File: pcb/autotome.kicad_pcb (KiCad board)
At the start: 2 copper layers, 61 parts, among them SW1 SW_PUSH, SW10 SW_PUSH, SW11 SW_PUSH, SW12 SW_PUSH, SW13 SW_PUSH, SW14 SW_PUSH, SW15 SW_PUSH, SW16 SW_PUSH, SW17 SW_PUSH, SW18 SW_PUSH, SW19 SW_PUSH, SW2 SW_PUSH, SW20 SW_PUSH, SW21 SW_PUSH, SW22 SW_PUSH, SW23 SW_PUSH, SW24 SW_PUSH, SW25 RotaryEncoder_Switch, SW27 SW_PUSH, SW28 SW_PUSH, SW29 SW_PUSH, SW3 SW_PUSH, SW30 SW_PUSH, SW31 SW_SPDT, SW4 SW_PUSH, SW5 SW_PUSH, SW6 SW_PUSH, SW7 SW_PUSH, SW8 SW_PUSH, SW9 SW_PUSH, U1 ProMicro

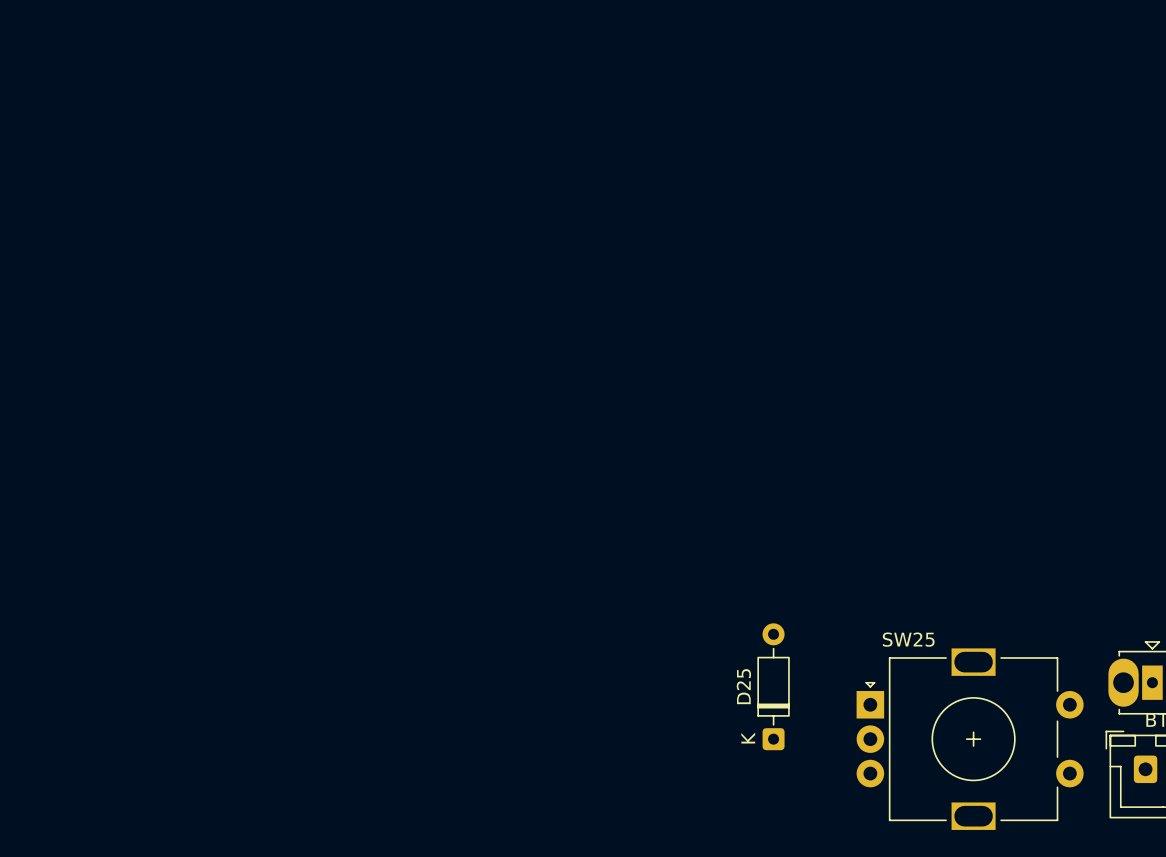
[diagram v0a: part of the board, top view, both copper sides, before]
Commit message: add rotary encoder 3d model and custom library
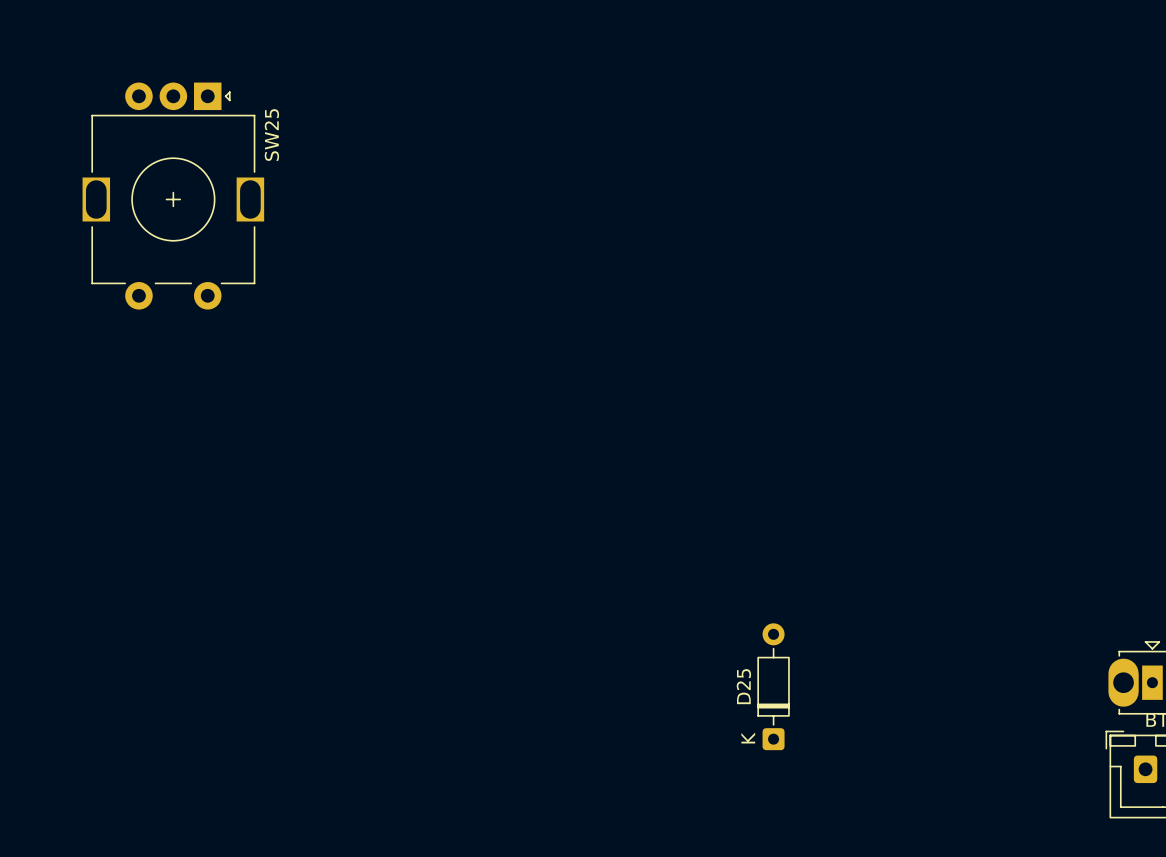
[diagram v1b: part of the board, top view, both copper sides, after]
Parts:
- SW25: footprint Rotary_Encoder:RotaryEncoder_Alps_EC11E-Switch_Vertical_H20mm -> my_library:RotaryEncoder_Alps_EC11E-Switch_Vertical_H20mm
- moved SW25 65.4 mm to (197.0, 115.2), turned to -90 degrees
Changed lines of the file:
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@@
 		(capping no)
 		(filling no)
+		(aux_axis_origin 123.14608 139.584744)
 		(pcbplotparams
 			(layerselection 0x00000000_00000000_55555555_5755f5ff)
@@
 		)
 	)
-	(footprint "Rotary_Encoder:RotaryEncoder_Alps_EC11E-Switch_Vertical_H20mm"
+	(footprint "my_library:RotaryEncoder_Alps_EC11E-Switch_Vertical_H20mm"
 		(layer "F.Cu")
-		(at 245.1625 159.425)
+		(at 197 115.2 -90)
 		(descr "Alps rotary encoder, EC11E... with switch, vertical shaft, http://www.alps.com/prod/info/E/HTML/Encoder/Incremental/EC11/EC11E15204A3.html")
 		(tags "rotary encoder")
 		(property "Reference" "SW25"
-			(at 2.8 -4.7 0)
+			(at 2.8 -4.7 270)
 			(layer "F.SilkS")
 			(effects
@@
 		)
 		(property "Value" "RotaryEncoder_Switch"
-			(at 7.5 10.4 0)
+			(at 7.5 10.4 270)
 			(layer "F.Fab")
 			(effects
@@
 		)
 		(property "Datasheet" ""
-			(at 0 0 0)
+			(at 0 0 270)
 			(unlocked yes)
 			(layer "F.Fab")
@@
 		)
 		(property "Description" "Rotary encoder, dual channel, incremental quadrate outputs, with switch"
-			(at 0 0 0)
+			(at 0 0 270)
 			(unlocked yes)
 			(layer "F.Fab")
@@
 		(duplicate_pad_numbers_are_jumpers no)
 		(fp_line
+			(start 5.5 8.4)
+			(end 1.4 8.4)
+			(stroke
+				(width 0.12)
+				(type solid)
+			)
+			(layer "F.SilkS")
+		)
+		(fp_line
+			(start 13.6 8.4)
+			(end 9.5 8.4)
+			(stroke
+				(width 0.12)
+				(type solid)
+			)
+			(layer "F.SilkS")
+		)
+		(fp_line
+			(start 13.6 6)
+			(end 13.6 8.4)
+			(stroke
+				(width 0.12)
+				(type solid)
+			)
+			(layer "F.SilkS")
+		)
+		(fp_line
+			(start 7 2.5)
+			(end 8 2.5)
+			(stroke
+				(width 0.12)
+				(type solid)
+			)
+			(layer "F.SilkS")
+		)
+		(fp_line
+			(start 7.5 2)
+			(end 7.5 3)
+			(stroke
+				(width 0.12)
+				(type solid)
+			)
+			(layer "F.SilkS")
+		)
+		(fp_line
+			(start 13.6 1.2)
+			(end 13.6 3.8)
+			(stroke
+				(width 0.12)
+				(type solid)
+			)
+			(layer "F.SilkS")
+		)
+		(fp_line
+			(start 0 -1.3)
+			(end -0.3 -1.6)
+			(stroke
+				(width 0.12)
+				(type solid)
+			)
+			(layer "F.SilkS")
+		)
+		(fp_line
 			(start -0.3 -1.6)
 			(end 0.3 -1.6)
@@
 		)
 		(fp_line
-			(start 0 -1.3)
-			(end -0.3 -1.6)
-			(stroke
-				(width 0.12)
-				(type solid)
-			)
-			(layer "F.SilkS")
-		)
-		(fp_line
 			(start 0.3 -1.6)
 			(end 0 -1.3)
@@
 		)
 		(fp_line
-			(start 5.5 8.4)
-			(end 1.4 8.4)
-			(stroke
-				(width 0.12)
-				(type solid)
-			)
-			(layer "F.SilkS")
-		)
-		(fp_line
-			(start 7 2.5)
-			(end 8 2.5)
-			(stroke
-				(width 0.12)
-				(type solid)
-			)
-			(layer "F.SilkS")
-		)
-		(fp_line
-			(start 7.5 2)
-			(end 7.5 3)
-			(stroke
-				(width 0.12)
-				(type solid)
-			)
-			(layer "F.SilkS")
-		)
-		(fp_line
 			(start 9.5 -3.4)
 			(end 13.6 -3.4)
@@
 			(start 13.6 -3.4)
 			(end 13.6 -1)
-			(stroke
-				(width 0.12)
-				(type solid)
-			)
-			(layer "F.SilkS")
-		)
-		(fp_line
-			(start 13.6 1.2)
-			(end 13.6 3.8)
-			(stroke
-				(width 0.12)
-				(type solid)
-			)
-			(layer "F.SilkS")
-		)
-		(fp_line
-			(start 13.6 6)
-			(end 13.6 8.4)
-			(stroke
-				(width 0.12)
-				(type solid)
-			)
-			(layer "F.SilkS")
-		)
-		(fp_line
-			(start 13.6 8.4)
-			(end 9.5 8.4)
 			(stroke
 				(width 0.12)
@@
 		)
 		(fp_line
+			(start 16 9.6)
+			(end -1.5 9.6)
+			(stroke
+				(width 0.05)
+				(type solid)
+			)
+			(layer "F.CrtYd")
+		)
+		(fp_line
+			(start 16 9.6)
+			(end 16 -4.6)
+			(stroke
+				(width 0.05)
+				(type solid)
+			)
+			(layer "F.CrtYd")
+		)
+		(fp_line
 			(start -1.5 -4.6)
 			(end -1.5 9.6)
@@
 		)
 		(fp_line
-			(start 16 9.6)
-			(end -1.5 9.6)
-			(stroke
-				(width 0.05)
-				(type solid)
-			)
-			(layer "F.CrtYd")
-		)
-		(fp_line
-			(start 16 9.6)
-			(end 16 -4.6)
-			(stroke
-				(width 0.05)
-				(type solid)
-			)
-			(layer "F.CrtYd")
+			(start 1.5 8.3)
+			(end 1.5 -2.2)
+			(stroke
+				(width 0.12)
+				(type solid)
+			)
+			(layer "F.Fab")
+		)
+		(fp_line
+			(start 13.5 8.3)
+			(end 1.5 8.3)
+			(stroke
+				(width 0.12)
+				(type solid)
+			)
+			(layer "F.Fab")
+		)
+		(fp_line
+			(start 4.5 2.5)
+			(end 10.5 2.5)
+			(stroke
+				(width 0.12)
+				(type solid)
+			)
+			(layer "F.Fab")
+		)
+		(fp_line
+			(start 7.5 -0.5)
+			(end 7.5 5.5)
+			(stroke
+				(width 0.12)
+				(type solid)
+			)
+			(layer "F.Fab")
 		)
 		(fp_line
@@
 		)
 		(fp_line
-			(start 1.5 8.3)
-			(end 1.5 -2.2)
-			(stroke
-				(width 0.12)
-				(type solid)
-			)
-			(layer "F.Fab")
-		)
-		(fp_line
 			(start 2.5 -3.3)
 			(end 13.5 -3.3)
@@
 		)
 		(fp_line
-			(start 4.5 2.5)
-			(end 10.5 2.5)
-			(stroke
-				(width 0.12)
-				(type solid)
-			)
-			(layer "F.Fab")
-		)
-		(fp_line
-			(start 7.5 -0.5)
-			(end 7.5 5.5)
-			(stroke
-				(width 0.12)
-				(type solid)
-			)
-			(layer "F.Fab")
-		)
-		(fp_line
 			(start 13.5 -3.3)
 			(end 13.5 8.3)
-			(stroke
-				(width 0.12)
-				(type solid)
-			)
-			(layer "F.Fab")
-		)
-		(fp_line
-			(start 13.5 8.3)
-			(end 1.5 8.3)
 			(stroke
 				(width 0.12)
@@
 		)
 		(fp_text user "${REFERENCE}"
-			(at 11.1 6.3 0)
+			(at 11.1 6.3 270)
 			(layer "F.Fab")
 			(effects
@@
 		)
 		(pad "A" thru_hole rect
-			(at 0 0)
+			(at 0 0 270)
 			(size 2 2)
 			(drill 1)
@@
 		)
 		(pad "B" thru_hole circle
-			(at 0 5)
+			(at 0 5 270)
 			(size 2 2)
 			(drill 1)
@@
 		)
 		(pad "C" thru_hole circle
-			(at 0 2.5)
+			(at 0 2.5 270)
 			(size 2 2)
 			(drill 1)
@@
 		)
 		(pad "MP" thru_hole rect
-			(at 7.5 -3.1)
+			(at 7.5 -3.1 270)
 			(size 3.2 2)
 			(drill oval 2.8 1.5)
@@
 		)
 		(pad "MP" thru_hole rect
-			(at 7.5 8.1)
+			(at 7.5 8.1 270)
 			(size 3.2 2)
 			(drill oval 2.8 1.5)
@@
 		)
 		(pad "S1" thru_hole circle
-			(at 14.5 5)
+			(at 14.5 5 270)
 			(size 2 2)
 			(drill 1)
@@
 		)
 		(pad "S2" thru_hole circle
-			(at 14.5 0)
+			(at 14.5 0 270)
 			(size 2 2)
 			(drill 1)
@@
 		)
 		(embedded_fonts no)
-		(model "${KICAD10_3DMODEL_DIR}/Rotary_Encoder.3dshapes/RotaryEncoder_Alps_EC11E-Switch_Vertical_H20mm.step"
+		(model "/home/frost/Downloads/EC11_Rotary_Encoder_Switched.step"
 			(offset
-				(xyz 0 0 0)
+				(xyz 7.55 -2.5 0)
 			)
 			(scale
@@
 			)
 			(rotate
-				(xyz 0 0 0)
-			)
-		)
+				(xyz -0 -0 90)
+			)
+		)

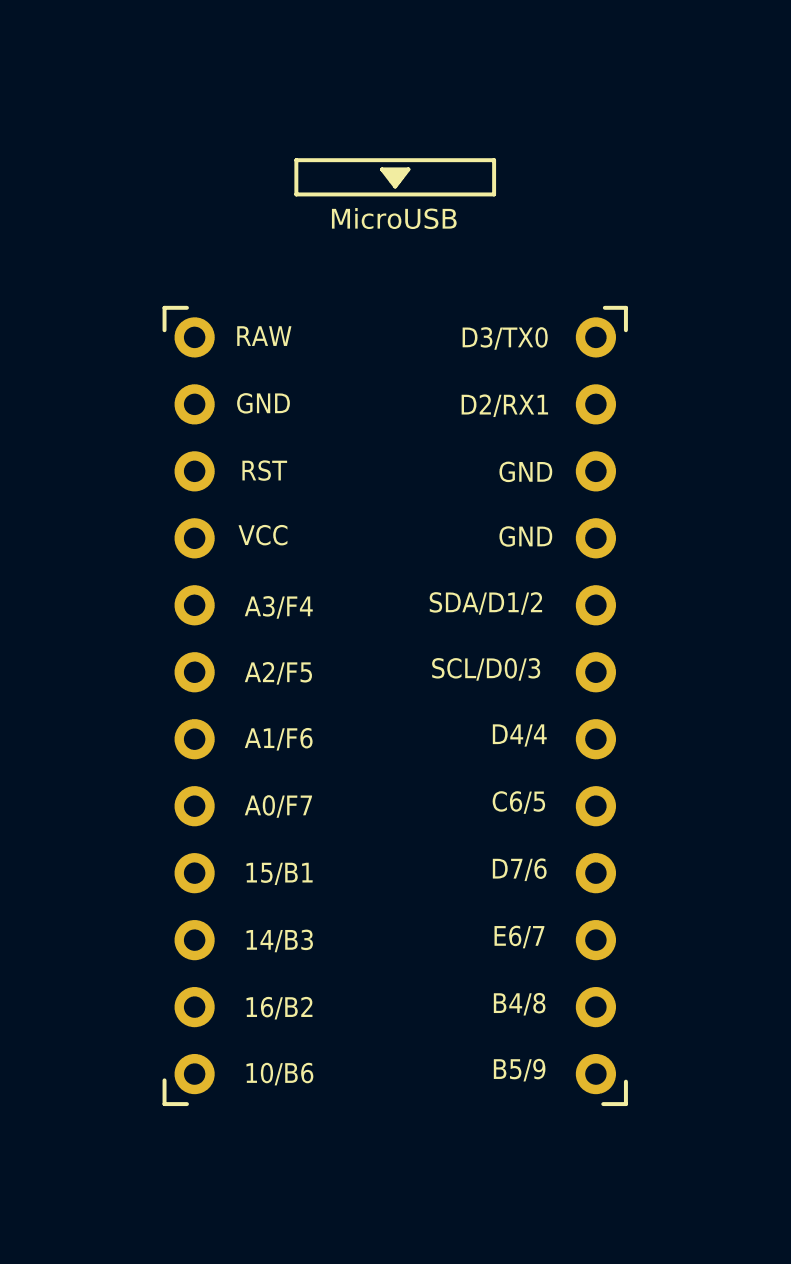
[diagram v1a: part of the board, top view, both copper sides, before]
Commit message: add nice nano 3d model with headers
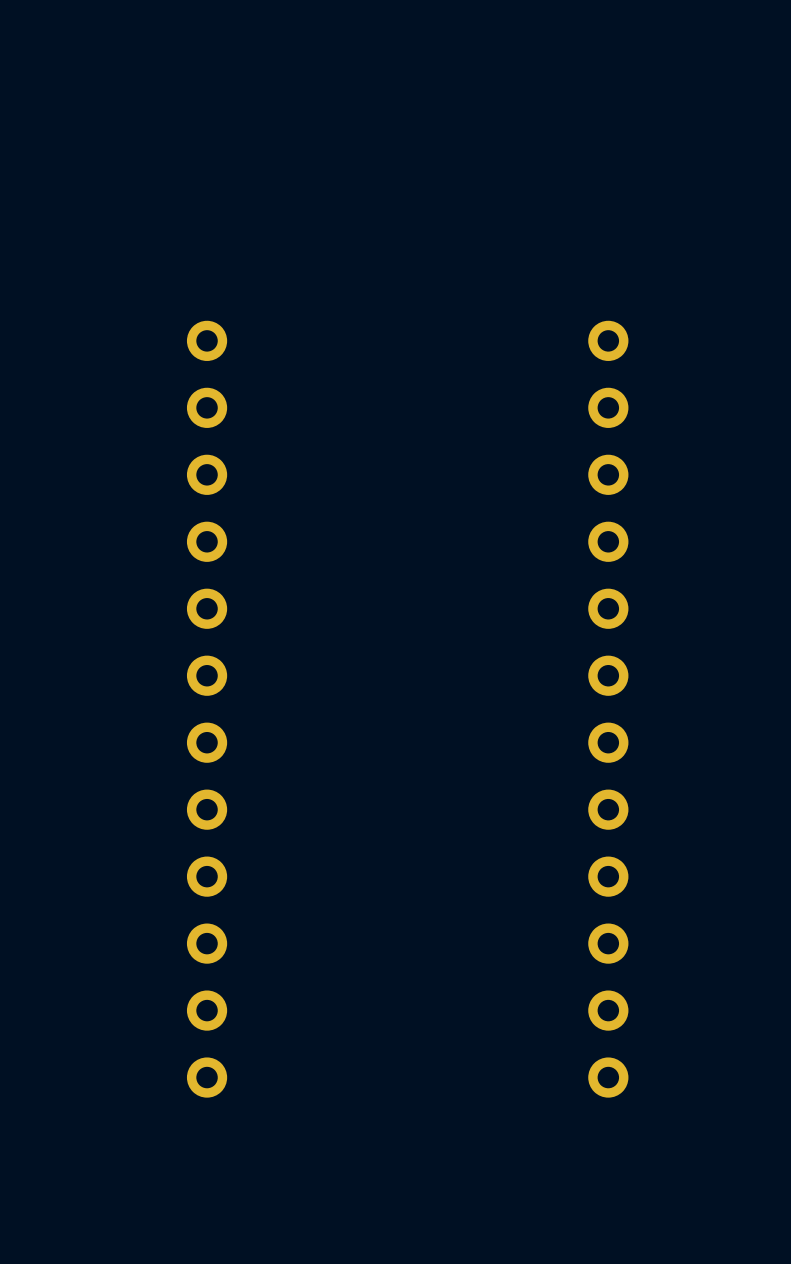
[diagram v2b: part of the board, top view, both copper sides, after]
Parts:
- SW25: footprint my_library:RotaryEncoder_Alps_EC11E-Switch_Vertical_H20mm -> autotome_library:RotaryEncoder_Alps_EC11E-Switch_Vertical_H20mm
- U1: footprint kbd:ProMicro -> autotome_library:NiceNano; moved to B.Cu
- moved U1 0.49 mm to (245.3, 77.5), turned to 180 degrees
